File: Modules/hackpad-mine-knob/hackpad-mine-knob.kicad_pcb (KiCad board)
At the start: 4 copper layers, 81.6 x 35.5 mm, 56 parts, among them J1 UPDI_Common, J2 Right_Connector, J3 Bottom_Connector, J4 Left_Connector, J5 Top_Connector, Q1 PMOS, SW1 RotaryEncoder_Switch, SW2 RotaryEncoder_Switch, SW3 RotaryEncoder_Switch, SW4 SW_SPDT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

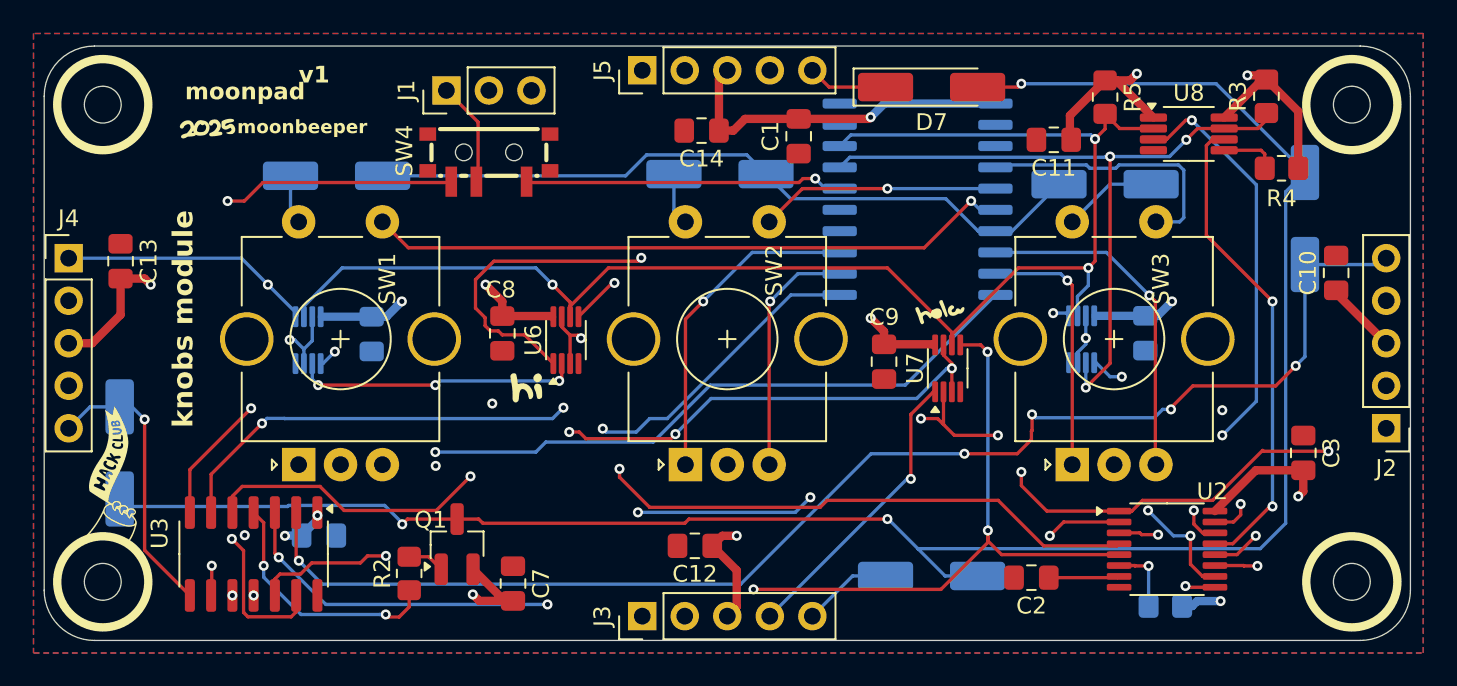
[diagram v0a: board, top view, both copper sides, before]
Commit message: updated pcb silkscreen for prettification
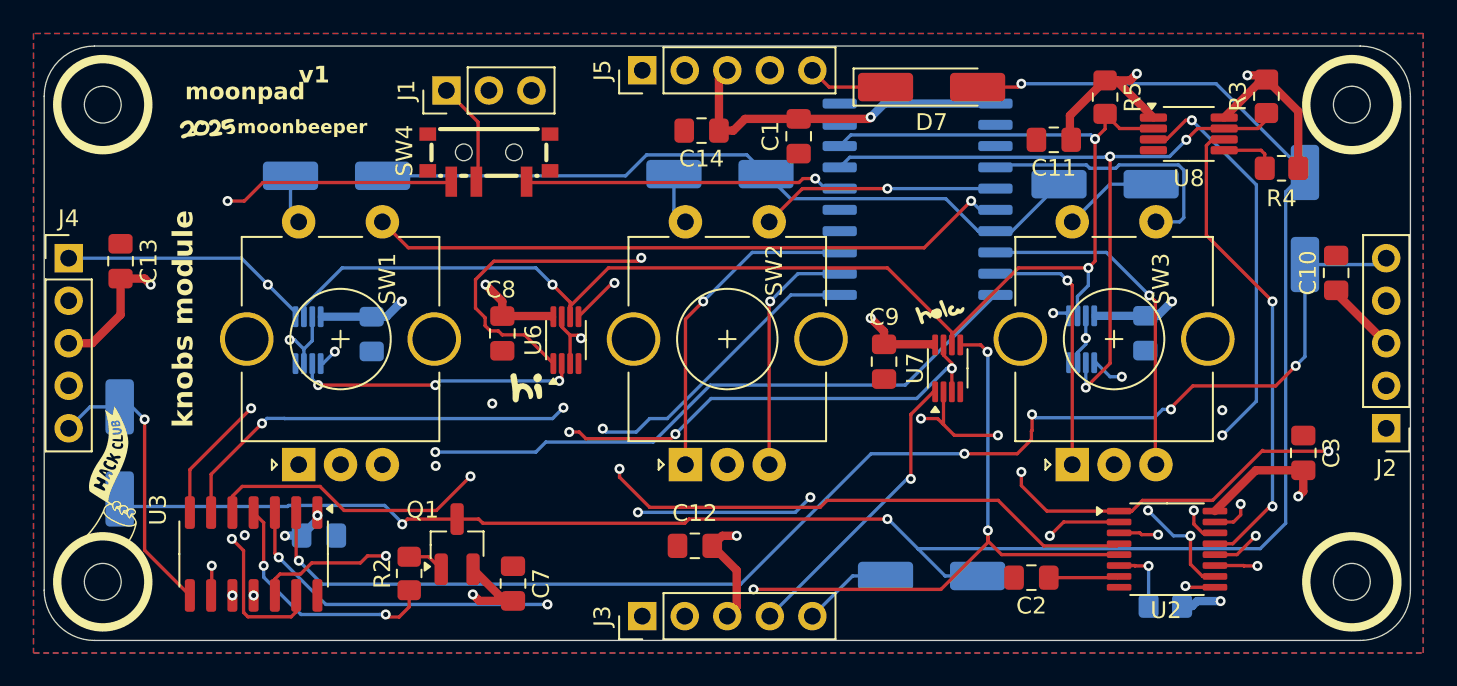
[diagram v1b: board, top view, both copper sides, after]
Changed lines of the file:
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@@
 		(tags "VSSOP SO JEDEC-MO-187-AA TI-DGK0008A")
 		(property "Reference" "U8"
-			(at 0 -2.45 0)
+			(at 0 2.65 0)
 			(layer "F.SilkS")
 			(effects
@@
 		(tags "SOIC SO")
 		(property "Reference" "U3"
-			(at -1.2375 5.610854 90)
+			(at -2.6375 5.710854 90)
 			(layer "F.SilkS")
 			(effects
@@
 		(tags "SOT-23 AO3401A")
 		(property "Reference" "Q1"
-			(at 1.45 -1.58 0)
+			(at 2.05 -2.0625 0)
 			(layer "F.SilkS")
 			(effects
@@
 		(tags "TSSOP SO JEDEC-MO-153-AB TI-PW0016A Microchip-ST Toshiba-TSSOP16-P-0044-0.65A NXP-SOT403-1 Infineon-P-TSSOP-16-800")
 		(property "Reference" "U2"
-			(at 2.7 -3.45 0)
+			(at -0.0625 3.65 0)
 			(layer "F.SilkS")
 			(effects
@@
 		(tags "capacitor handsolder")
 		(property "Reference" "C12"
-			(at 0 -1.68 0)
+			(at 0 1.95 0)
 			(layer "F.SilkS")
 			(effects
